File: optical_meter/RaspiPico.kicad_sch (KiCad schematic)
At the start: 7 parts, among them J4 Conn_02x03, U4 Pico

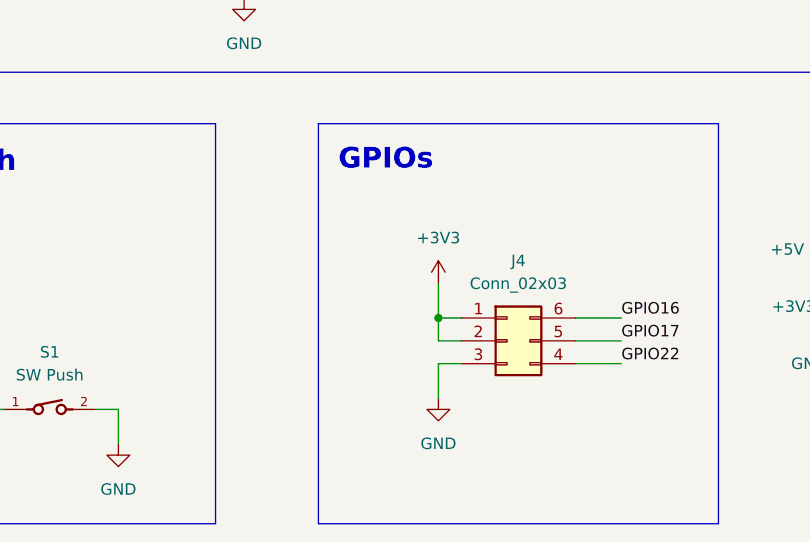
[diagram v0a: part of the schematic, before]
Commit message: Fixed pullup connections at TX_FAULT and R_LOS pins
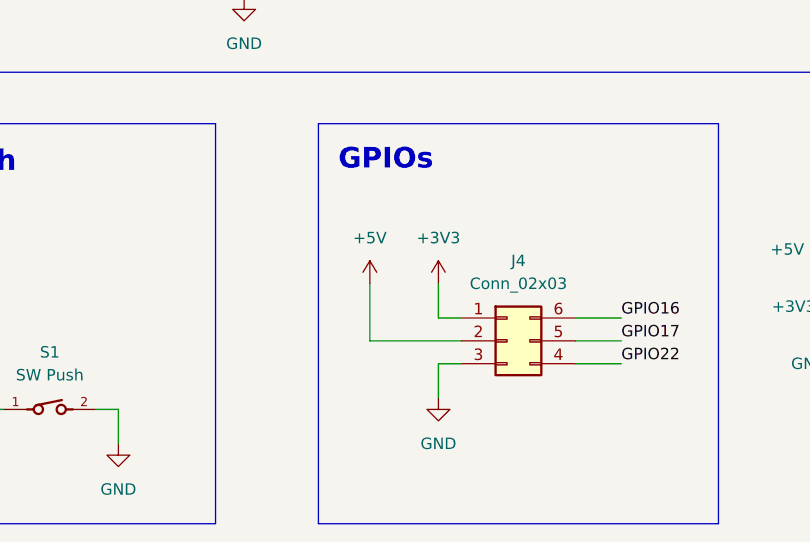
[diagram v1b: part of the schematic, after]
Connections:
- net +3V3: no longer J4.2 (Pin_2)
- net +5V: now also J4.2 (Pin_2)
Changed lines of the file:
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@@
-	)
-	(junction
-		(at 133.35 142.24)
-		(diameter 0)
-		(color 0 0 0 0)
 	)
 	(junction
@@
 	(wire
 		(pts
-			(xy 133.35 144.78) (xy 133.35 142.24)
-		)
-		(stroke
-			(width 0)
-			(type default)
-		)
-	)
-	(wire
-		(pts
 			(xy 148.59 144.78) (xy 153.67 144.78)
 		)
@@
 	(wire
 		(pts
-			(xy 135.89 144.78) (xy 133.35 144.78)
-		)
-		(stroke
-			(width 0)
-			(type default)
-		)
-	)
-	(wire
-		(pts
 			(xy 129.54 52.07) (xy 138.43 52.07)
 		)
@@
 	(wire
 		(pts
+			(xy 135.89 144.78) (xy 125.73 144.78)
+		)
+		(stroke
+			(width 0)
+			(type default)
+		)
+	)
+	(wire
+		(pts
 			(xy 129.54 77.47) (xy 139.7 77.47)
 		)
@@
 		(pts
 			(xy 129.54 62.23) (xy 161.29 62.23)
+		)
+		(stroke
+			(width 0)
+			(type default)
+		)
+	)
+	(wire
+		(pts
+			(xy 125.73 144.78) (xy 125.73 138.43)
 		)
 		(stroke
@@
 					(unit 1)
 				)
+			)
+		)
+	)
+	(symbol
+		(lib_id "power:+5V")
+		(at 125.73 138.43 0)
+		(unit 1)
+		(exclude_from_sim no)
+		(in_bom yes)
+		(on_board yes)
+		(dnp no)
+		(fields_autoplaced yes)
+		(property "Reference" "#PWR056"
+			(at 125.73 142.24 0)
+			(effects
+				(font
+					(size 1.27 1.27)
+				)
+				(hide yes)
+			)
+		)
+		(property "Value" "+5V"
+			(at 125.73 133.35 0)
+			(effects
+				(font
+					(size 1.27 1.27)
+				)
+			)
+		)
+		(property "Footprint" ""
+			(at 125.73 138.43 0)
+			(effects
+				(font
+					(size 1.27 1.27)
+				)
+				(hide yes)
+			)
+		)
+		(property "Datasheet" ""
+			(at 125.73 138.43 0)
+			(effects
+				(font
+					(size 1.27 1.27)
+				)
+				(hide yes)
+			)
+		)
+		(property "Description" "Power symbol creates a global label with name \"+5V\""
+			(at 125.73 138.43 0)
+			(effects
+				(font
+					(size 1.27 1.27)
+				)
+				(hide yes)
+			)
+		)
+		(pin "1"
+		)
+		(instances
+			(project "optical_meter"
+				(path "/329e6fb6-763d-4479-a593-6f78470800a1/a30fce3a-b9ac-4590-ae34-4ac7fee85d9a"
+					(reference "#PWR056")
+					(unit 1)
+				)
